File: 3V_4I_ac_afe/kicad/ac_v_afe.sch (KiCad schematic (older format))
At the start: 20 parts, among them J10 screw, J11 V_ref, J12 VDDA, J13 SIGNAL, J14 GNDA, J8 AC L, J9 AC N, U2 MCP6021T

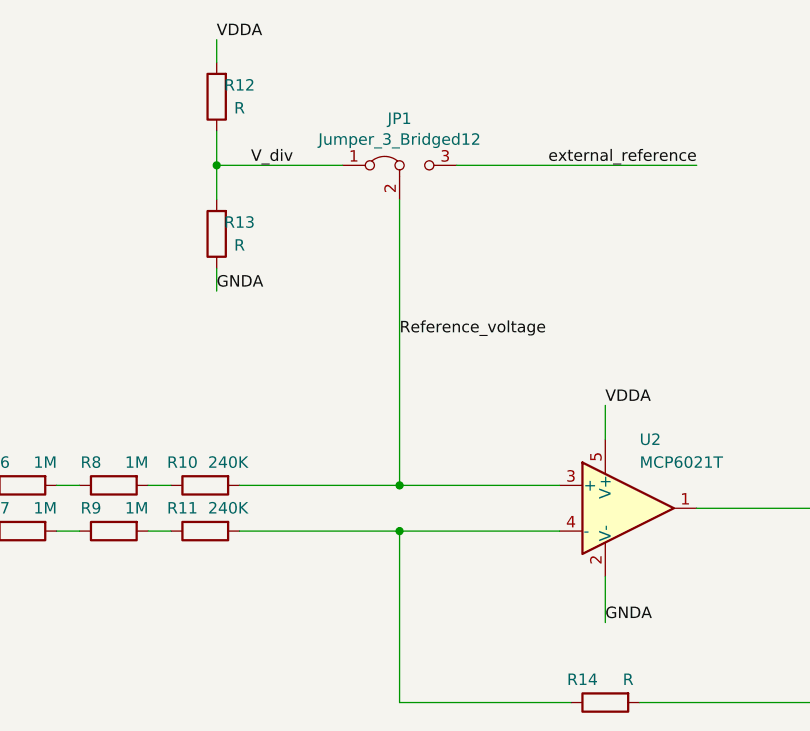
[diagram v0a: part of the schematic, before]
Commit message: added few prototypes and script for zipping kicad gerbers
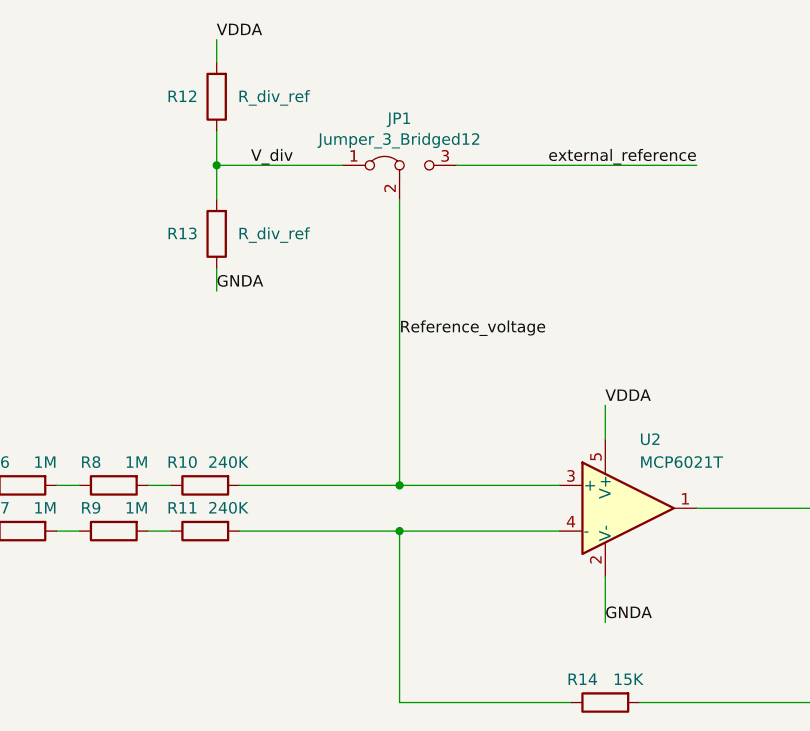
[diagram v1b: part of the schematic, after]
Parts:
- R12, R13: value R -> R_div_ref
- R14: value R -> 15K
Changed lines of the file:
@@
 AR Path="/5FA5EA5F/5FA43B3C" Ref="R36"  Part="1"
 F 0 "R14" V 5950 5200 50  0000 C CNN
-F 1 "R" V 5950 5000 50  0000 C CNN
+F 1 "15K" V 5950 5000 50  0000 C CNN
 F 2 "Resistor_SMD:R_0805_2012Metric" V 5980 5100 50  0001 C CNN
 F 3 "~" H 6050 5100 50  0001 C CNN
@@
 AR Path="/5FA5E85E/5FA3F818" Ref="R24"  Part="1"
 AR Path="/5FA5EA5F/5FA3F818" Ref="R35"  Part="1"
-F 0 "R13" H 4250 3000 50  0000 C CNN
-F 1 "R" H 4250 3100 50  0000 C CNN
+F 0 "R13" H 4500 3050 50  0000 C CNN
+F 1 "R_div_ref" H 4100 3050 50  0000 C CNN
 F 2 "Resistor_SMD:R_1206_3216Metric" V 4280 3050 50  0001 C CNN
 F 3 "~" H 4350 3050 50  0001 C CNN
@@
 AR Path="/5FA5E85E/5FA3E5DC" Ref="R23"  Part="1"
 AR Path="/5FA5EA5F/5FA3E5DC" Ref="R34"  Part="1"
-F 0 "R12" H 4250 2400 50  0000 C CNN
-F 1 "R" H 4250 2500 50  0000 C CNN
+F 0 "R12" H 4500 2450 50  0000 C CNN
+F 1 "R_div_ref" H 4100 2450 50  0000 C CNN
 F 2 "Resistor_SMD:R_1206_3216Metric" V 4280 2450 50  0001 C CNN
 F 3 "~" H 4350 2450 50  0001 C CNN
